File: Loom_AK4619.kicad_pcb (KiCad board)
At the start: 2 copper layers, 110 x 110 mm, 193 parts, among them J1 Conn_01x40, J2 Conn_01x40, U1 AK4619VN, U101 HT75xx-1-SOT89, U2 AK4619VN, U3 OPA1679, U4 OPA1679, U5 OPA1679, U6 OPA1679

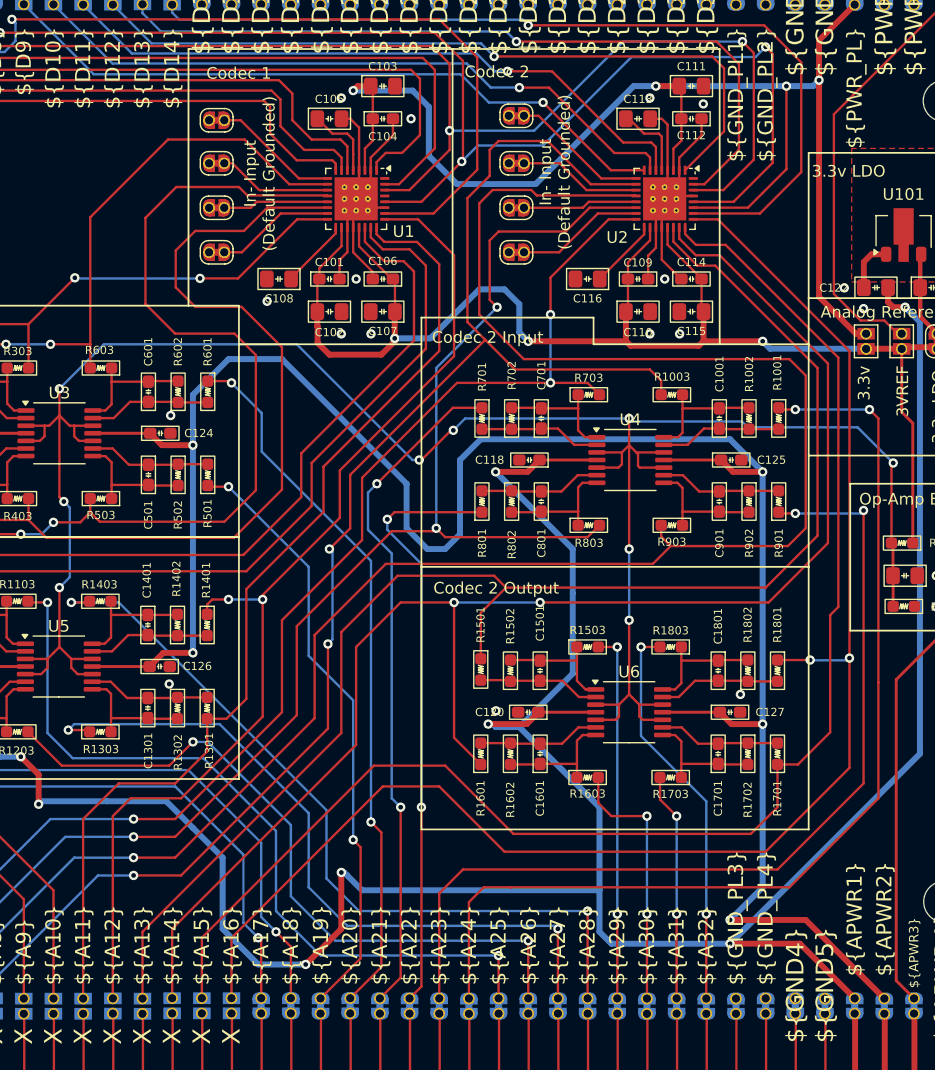
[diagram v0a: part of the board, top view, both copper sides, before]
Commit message: Slight routing updates
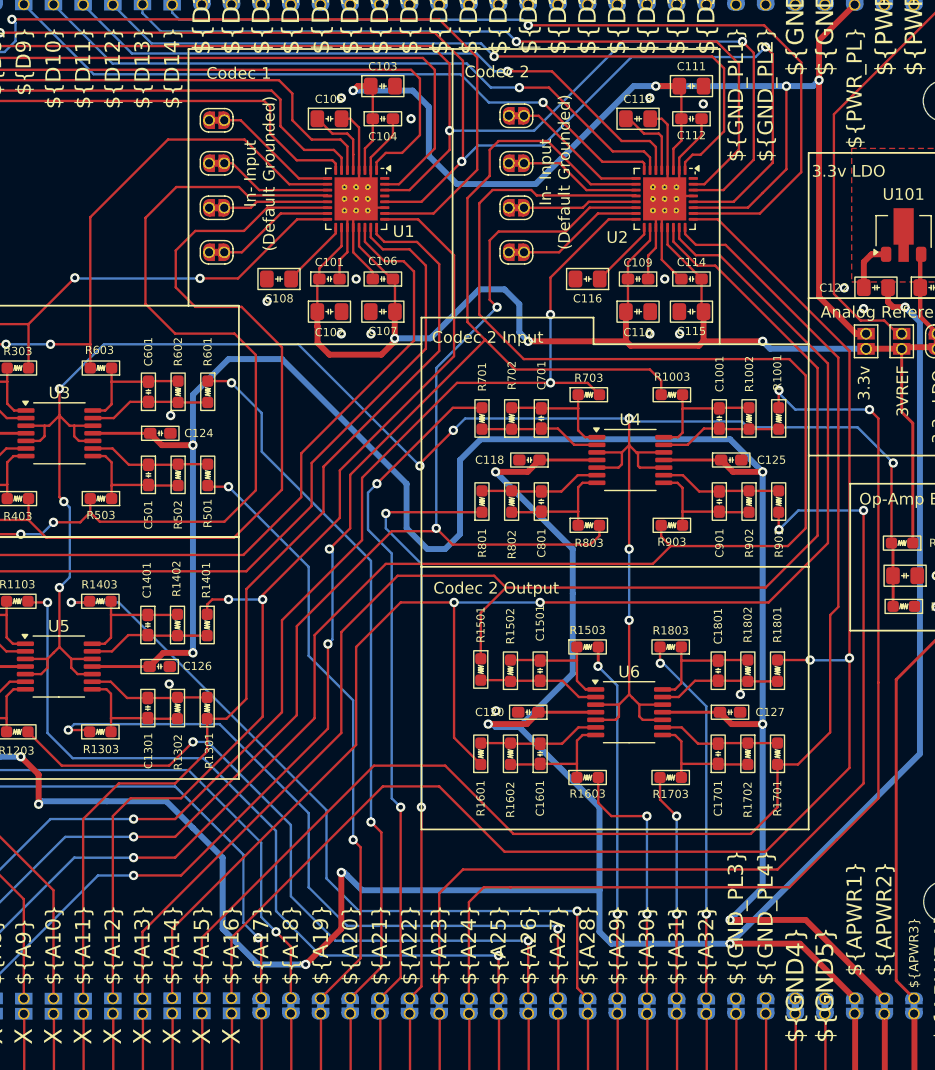
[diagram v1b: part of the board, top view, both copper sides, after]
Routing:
- net A24: track 88.4 -> 90.7 mm
- net A32: track 34.0 -> 31.9 mm
- net A23: track 80.0 -> 82.0 mm
- net A6: track 121.1 -> 122.1 mm
- net A29: track 31.7 -> 30.8 mm
- net Bias_VREF: track 188.6 -> 189.2 mm
- net A28: track 67.7 -> 67.1 mm

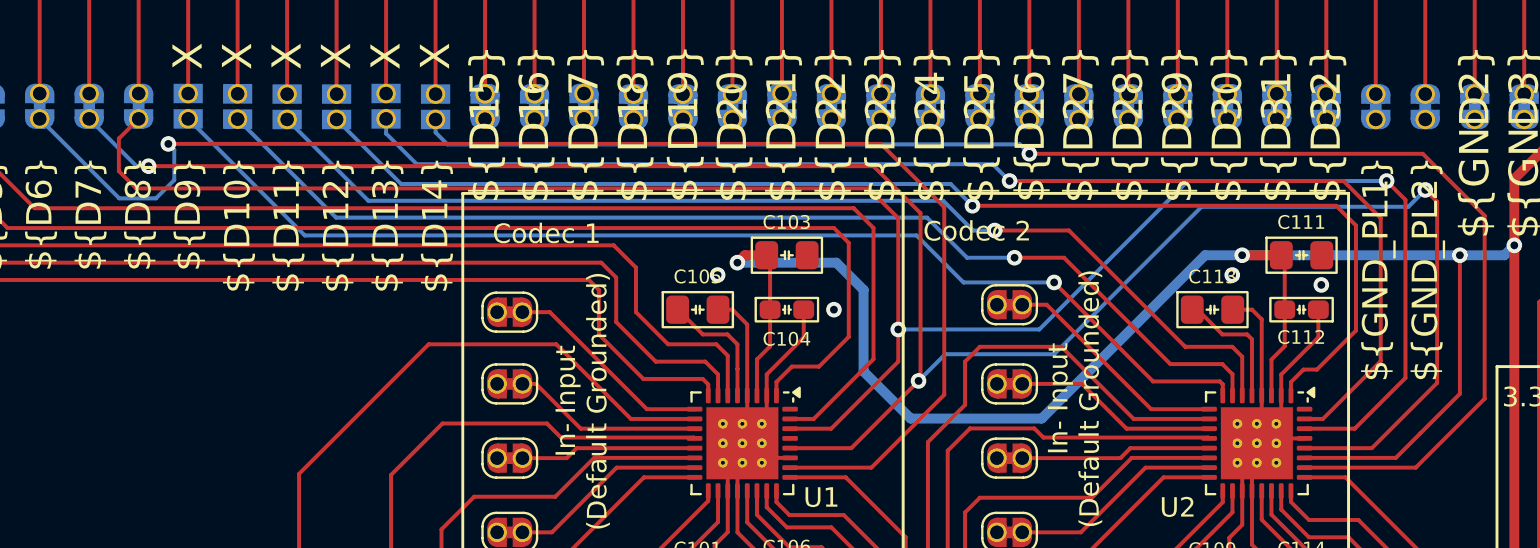
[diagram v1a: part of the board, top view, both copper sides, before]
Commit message: Added 33R resistors to SDOUT
Added 33R resistors to SDOUT to decrease slew rate slightly to reduce radiated emissions.
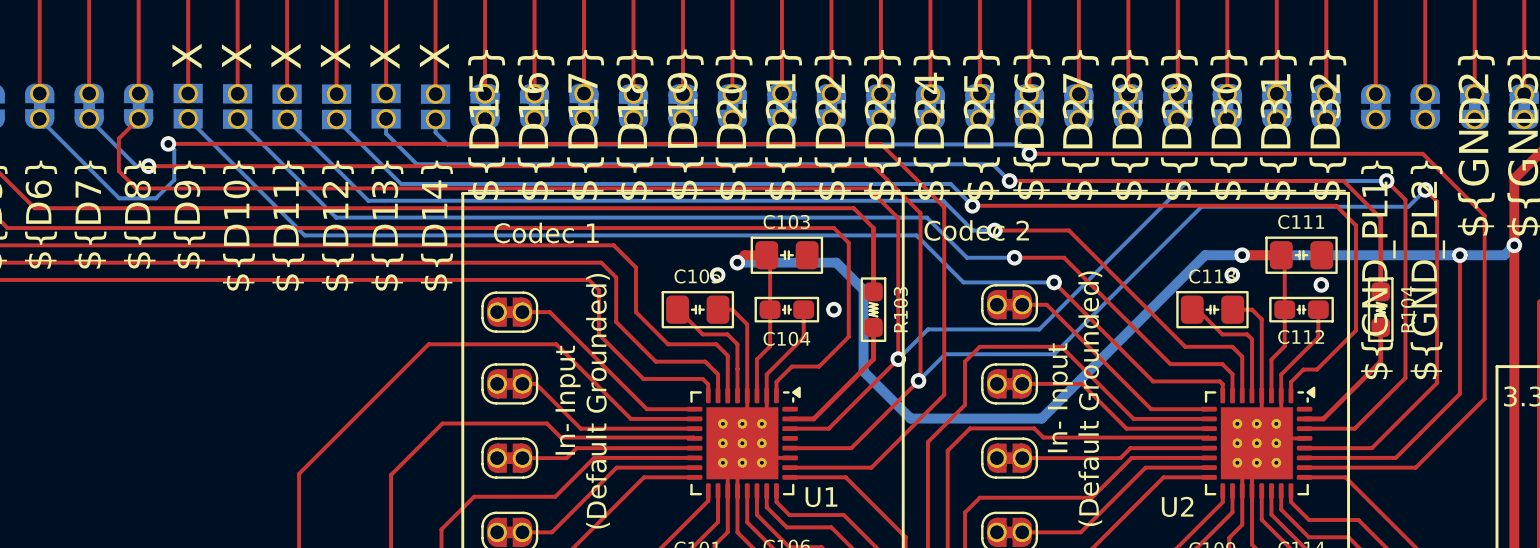
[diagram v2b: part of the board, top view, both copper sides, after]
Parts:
- added R103: 33R, winterbloom:R_0603_HandSolder, F.Cu at (134.9, 60.4)
- added R104: 33R, winterbloom:R_0603_HandSolder, F.Cu at (161.0, 60.4)
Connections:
- U1 pad 31: Codec1_TDM_RX -> Net-(U1-SDOUT1)
- U2 pad 31: Codec2_TDM_RX -> Net-(U2-SDOUT1)
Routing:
- net Codec1_TDM_RX: track 61.3 -> 52.3 mm
- net Codec2_TDM_RX: track 66.1 -> 57.4 mm
- net Net-(U1-SDOUT1): track 0.00 -> 7.18 mm
- net Net-(U2-SDOUT1): track 0.00 -> 6.88 mm
- net D8: track 103.4 -> 104.0 mm
